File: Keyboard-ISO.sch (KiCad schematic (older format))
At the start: 8 parts, among them J1 DB25_Female, J2 Conn_01x01_Female, J3 Conn_01x01_Female, J4 Conn_01x01_Female, J5 Conn_01x01_Female

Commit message: Add files via upload
updated files, and added pictures of PCB and key layouts
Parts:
- renumbered J4 to J2, J2 to J3, J5 to J4, J3 to J5
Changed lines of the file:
@@
 	8600 4400 8600 4600
 $Comp
-L Connector:Conn_01x01_Female J2
+L Connector:Conn_01x01_Female J3
 U 1 1 5F4352F7
 P 7400 5100
-F 0 "J2" H 7292 4875 50  0000 C CNN
+F 0 "J3" H 7292 4875 50  0000 C CNN
 F 1 "Conn_01x01_Female" H 7292 4966 50  0000 C CNN
 F 2 "MountingHole:MountingHole_4.5mm_Pad" H 7400 5100 50  0001 C CNN
@@
 	8250 5100 8250 4900
 $Comp
-L Connector:Conn_01x01_Female J3
+L Connector:Conn_01x01_Female J5
 U 1 1 5F442015
 P 7400 5450
-F 0 "J3" H 7292 5225 50  0000 C CNN
+F 0 "J5" H 7292 5225 50  0000 C CNN
 F 1 "Conn_01x01_Female" H 7292 5316 50  0000 C CNN
 F 2 "MountingHole:MountingHole_4.5mm_Pad" H 7400 5450 50  0001 C CNN
@@
 $EndComp
 $Comp
-L Connector:Conn_01x01_Female J5
+L Connector:Conn_01x01_Female J4
 U 1 1 5F444A6B
 P 9550 5200
-F 0 "J5" H 9442 4975 50  0000 C CNN
+F 0 "J4" H 9442 4975 50  0000 C CNN
 F 1 "Conn_01x01_Female" H 9442 5066 50  0000 C CNN
 F 2 "MountingHole:MountingHole_4.5mm_Pad" H 9550 5200 50  0001 C CNN
@@
 $EndComp
 $Comp
-L Connector:Conn_01x01_Female J4
+L Connector:Conn_01x01_Female J2
 U 1 1 5F444A76
 P 9550 4850
-F 0 "J4" H 9442 4625 50  0000 C CNN
+F 0 "J2" H 9442 4625 50  0000 C CNN
 F 1 "Conn_01x01_Female" H 9442 4716 50  0000 C CNN
 F 2 "MountingHole:MountingHole_4.5mm_Pad" H 9550 4850 50  0001 C CNN

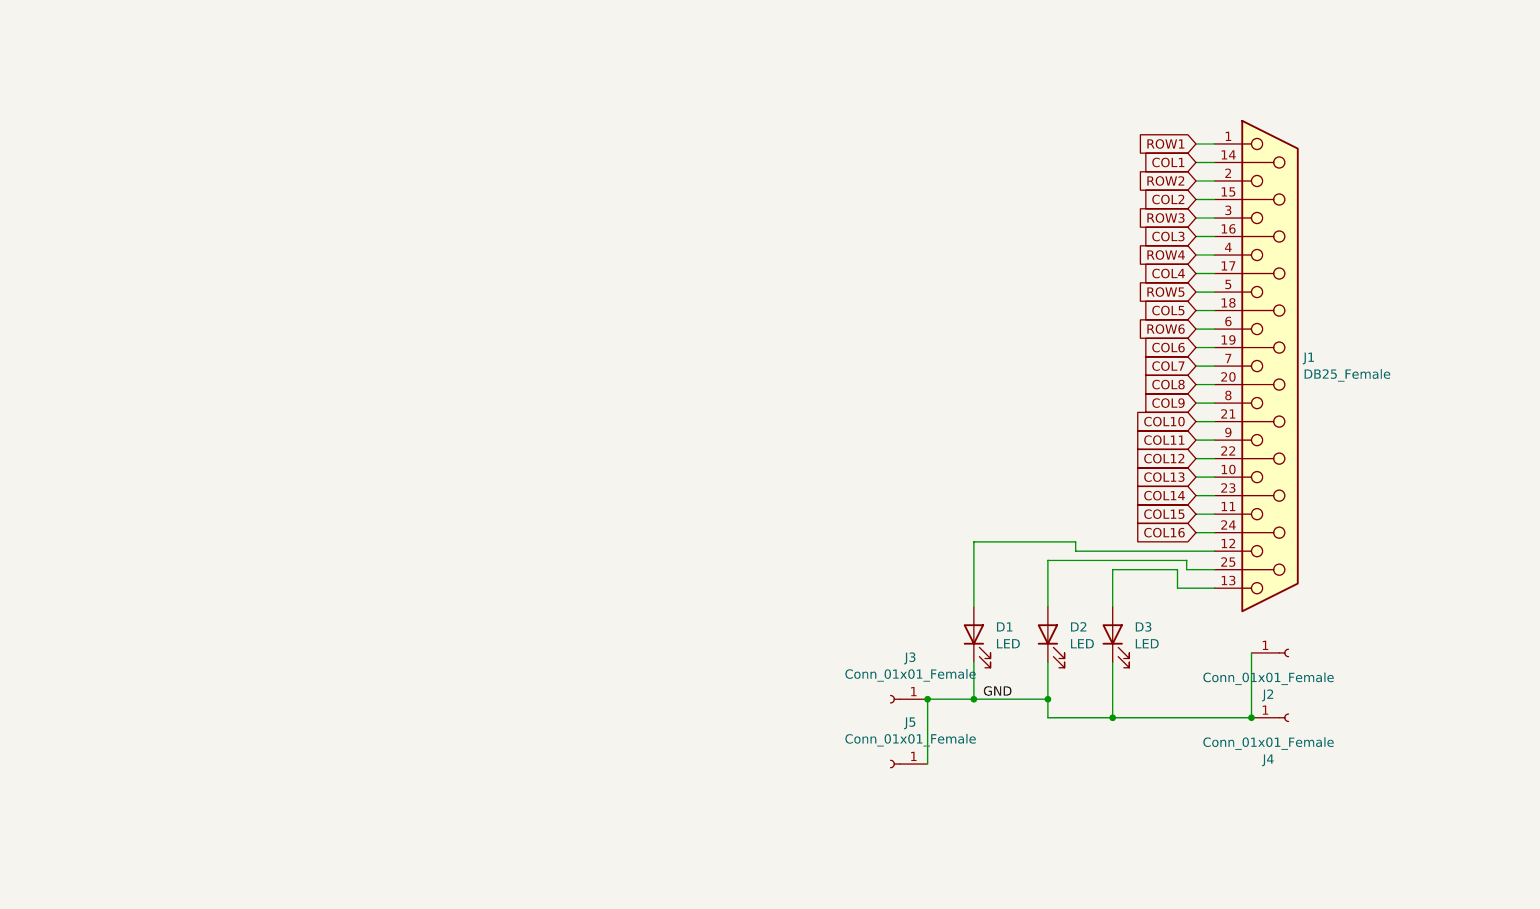
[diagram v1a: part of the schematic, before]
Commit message: updated files
Updated files, changed to using a Teensy++2.0 that plugs right in to the board
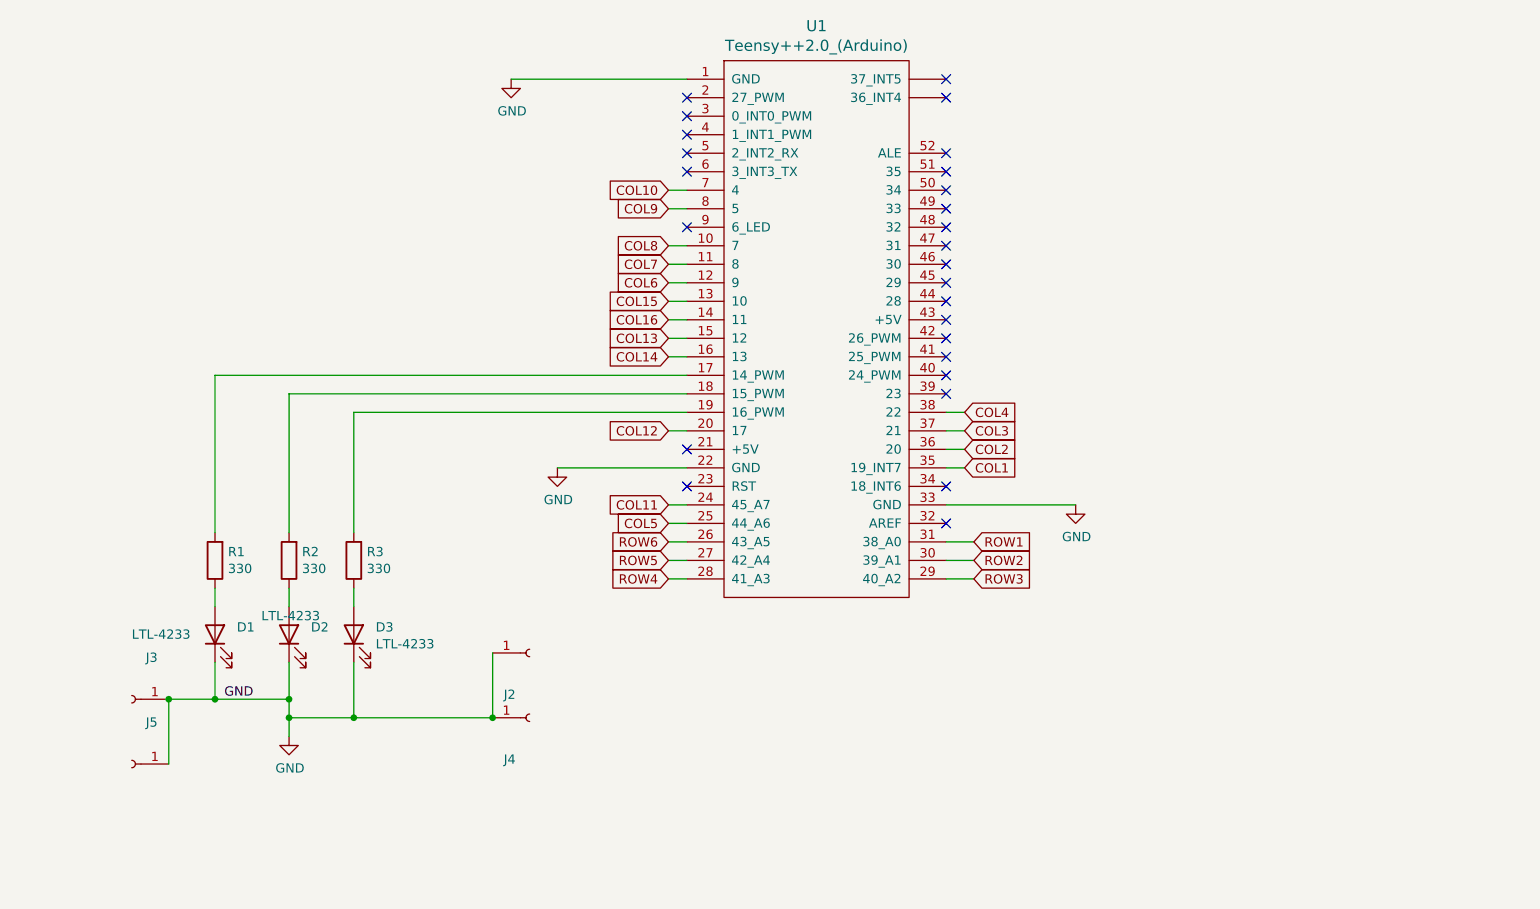
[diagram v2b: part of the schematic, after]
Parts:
- removed J1: DB25_Female, Connector_Dsub:DSUB-25_Female_Vertical_P2.77x2.84mm_MountingHoles, symbol Connector:DB25_Female
- added R1, R2, R3: 330, Resistor_THT:R_Axial_DIN0204_L3.6mm_D1.6mm_P5.08mm_Horizontal, symbol Device:R
- added U1: Teensy++2.0_(Arduino), Teensy:Teensy2.0-pins-headers, symbol Teensy:Teensy++2.0_(Arduino)
- D1, D2, D3: value LED -> LTL-4233
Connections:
- net COL1: now also U1.35 (19_INT7)
- net COL10: now also U1.7 (4)
- net COL11: now also U1.24 (45_A7)
- net COL12: now also U1.20 (17)
- net COL13: now also U1.15 (12)
- net COL14: now also U1.16 (13)
- net COL15: now also U1.13 (10)
- net COL16: now also U1.14 (11)
- net COL2: now also U1.36 (20)
- net COL3: now also U1.37 (21)
- net COL4: now also U1.38 (22)
- net COL5: now also U1.25 (44_A6)
- net COL6: now also U1.12 (9)
- net COL7: now also U1.11 (8)
- net COL8: now also U1.10 (7)
- net COL9: now also U1.8 (5)
- net GND: now also U1.1 (GND), U1.22 (GND), U1.33 (GND)
- net ROW1: now also U1.31 (38_A0)
- net ROW2: now also U1.30 (39_A1)
- net ROW3: now also U1.29 (40_A2)
- net ROW4: now also U1.28 (41_A3)
- net ROW5: now also U1.27 (42_A4)
- net ROW6: now also U1.26 (43_A5)
- net at D1.2 (A): now also R1.1
- net at D3.2 (A): now also R3.1
- net at D2.2 (A): now also R2.1
- new net: R1.2, U1.17 (14_PWM)
- new net: R2.2, U1.18 (15_PWM)
- new net: R3.2, U1.19 (16_PWM)
- no-connect marks 0 -> 26
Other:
- moved on the sheet: D1, D2, D3, J2, J3, J4, J5
